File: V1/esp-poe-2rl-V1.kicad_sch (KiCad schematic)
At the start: 56 parts, among them J1 USB_C_Receptacle_USB2.0, J2 RJ45 JACK, J3 1x2P 5,08mm, J4 1x2P 5,08mm, K1 G5NB-1A-E-DC5, K2 G5NB-1A-E-DC5, Q1 UMH3N, Q2 WPM2015-3/TR, Q3 LMUN2211LT1G, Q4 MMBT2222A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

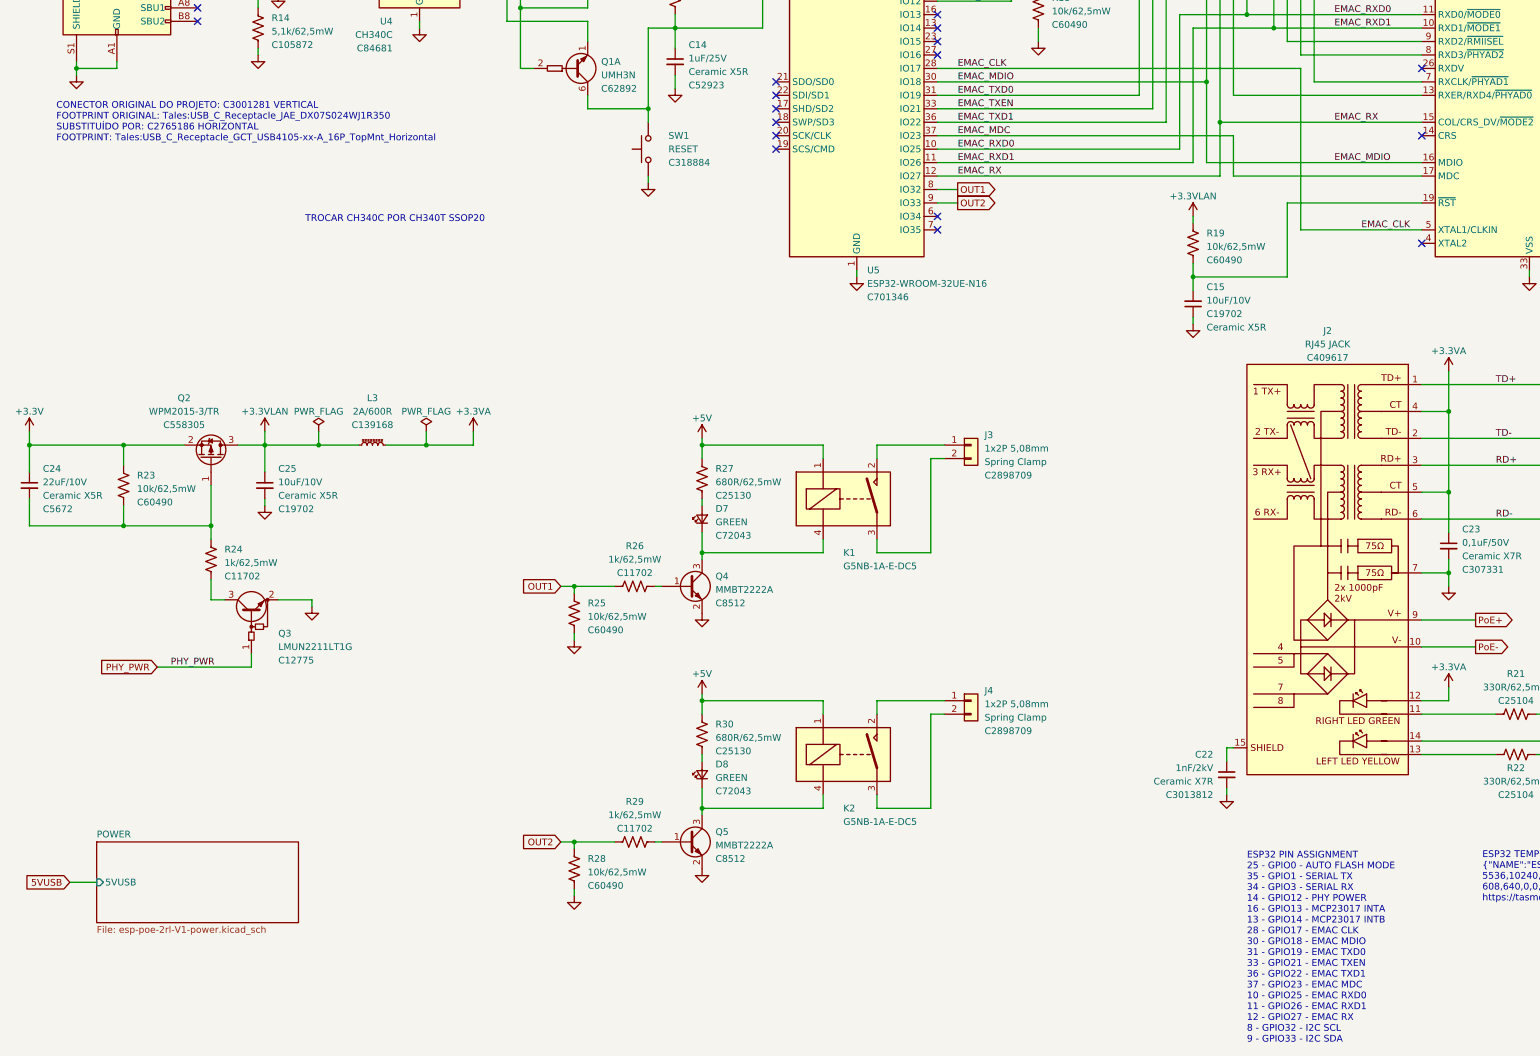
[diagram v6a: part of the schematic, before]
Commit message: Migrating layout to 4 layers
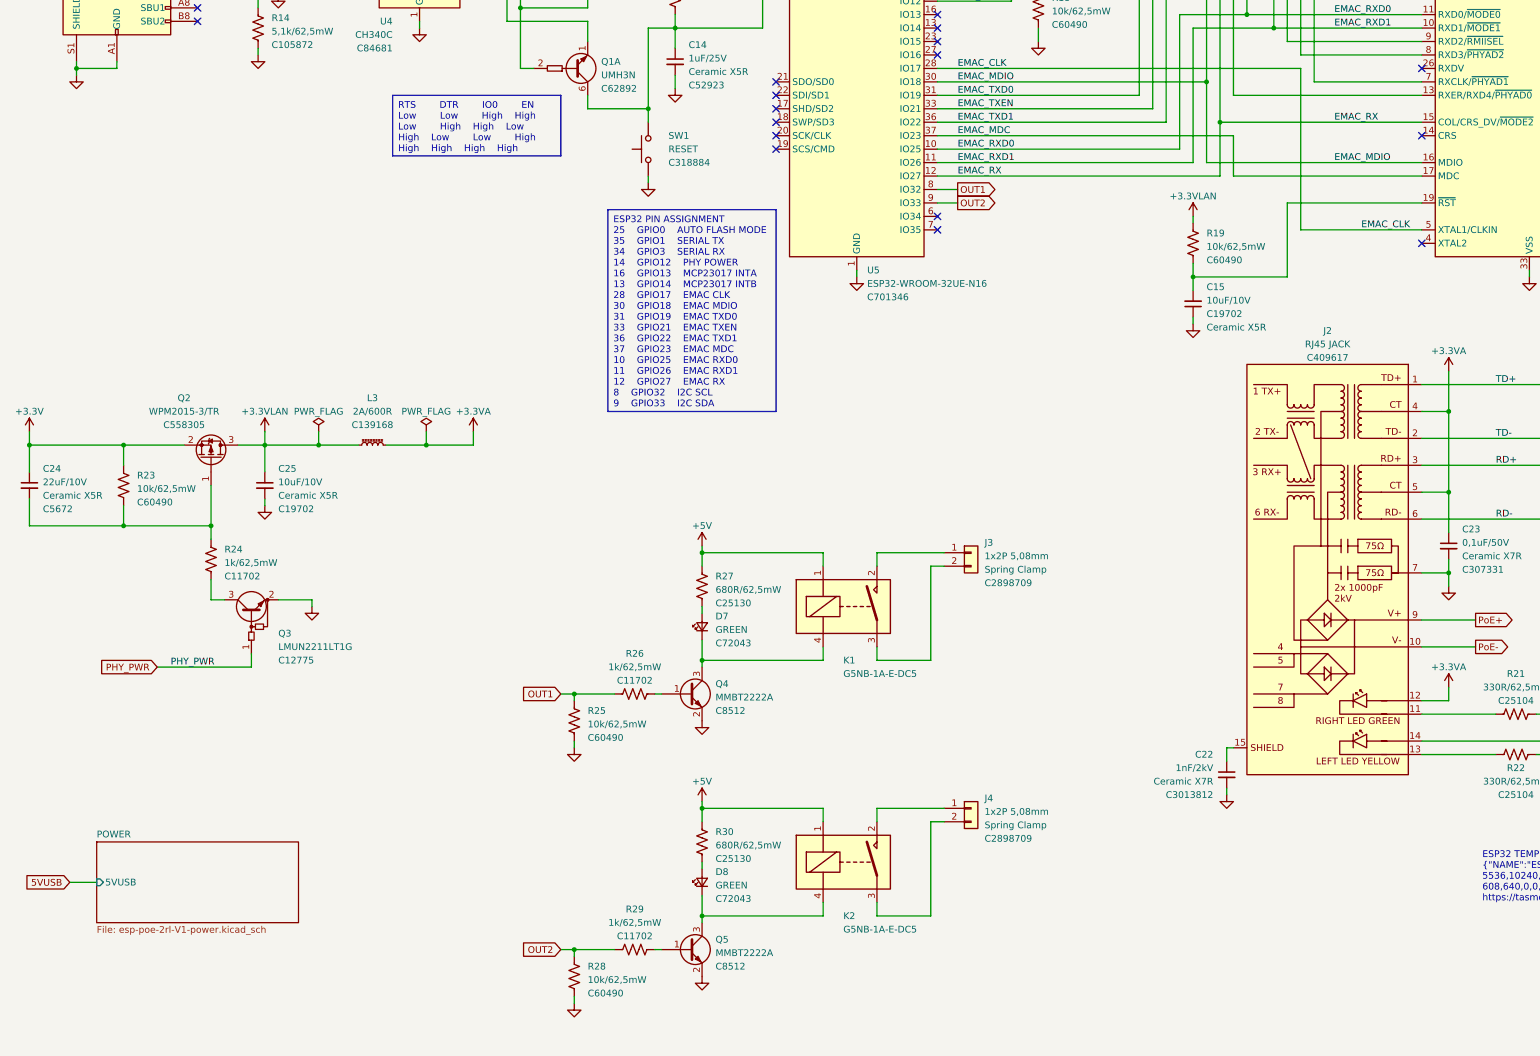
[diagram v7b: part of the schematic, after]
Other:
- note removed: "CONECTOR ORIGINAL DO PROJETO: C3001281 VERTICAL FOOTPRINT ORIGINAL: Tales:USB_C_Receptacle_JAE_DX07S024WJ1R350 SUBSTITUÍDO POR: C2765186 HORIZONTAL FOOTPRINT: Tales:USB_C_Receptacle_GCT_USB4105-xx-A_16P_TopMnt_Horizontal"
- note removed: "ESP32 PIN ASSIGNMENT 25 - GPIO0 - AUTO FLASH MODE 35 - GPIO1 - SERIAL TX 34 - GPIO3 - SERIAL RX 14 - GPIO12 - PHY POWER 16 - GPIO13 - MCP23017 INTA 13 - GPIO14 - MCP23017 INTB 28 - GPIO17 - EMAC CLK 30 - GPIO18 - EMAC MDIO 31 - GPIO19 - EMAC TXD0 33 - GPIO21 - EMAC TXEN 36 - GPIO22 - EMAC TXD1 37 - GPIO23 - EMAC MDC 10 - GPIO25 - EMAC RXD0 11 - GPIO26 - EMAC RXD1 12 - GPIO27 - EMAC RX 8 - GPIO32 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"
- note removed: "TROCAR CH340C POR CH340T SSOP20"
- moved on the sheet: D7, D8, J3, J4, K1, K2, Q4, Q5, R25, R26, R27, R28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

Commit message: PCB dev
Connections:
- net +3.3VLAN: now also RN1.6 (R3.2); no longer RN1.5 (R4.2)
- net EMAC_RXD0: now also RN1.3 (R3.1); no longer RN1.4 (R4.1)
- net GND: now also RN1.5 (R4.2); no longer RN1.6 (R3.2)
- net at U6.13 (RXER/RXD4/~{PHYAD0}): now also RN1.4 (R4.1); no longer RN1.3 (R3.1)
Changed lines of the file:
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@@
   (junction (at 359.41 85.09) (diameter 0) (color 0 0 0 0)
   )
+  (junction (at 252.73 46.99) (diameter 0) (color 0 0 0 0)
+  )
   (junction (at 128.27 259.08) (diameter 0) (color 0 0 0 0)
   )
@@
   (junction (at 317.5 29.21) (diameter 0) (color 0 0 0 0)
   )
+  (junction (at 252.73 82.55) (diameter 0) (color 0 0 0 0)
+  )
   (junction (at 245.11 132.08) (diameter 0) (color 0 0 0 0)
   )
@@
   (junction (at 311.15 46.99) (diameter 0) (color 0 0 0 0)
   )
-  (junction (at 255.27 82.55) (diameter 0) (color 0 0 0 0)
-  )
   (junction (at 63.5 40.64) (diameter 0) (color 0 0 0 0)
   )
@@
   )
   (junction (at 387.35 142.24) (diameter 0) (color 0 0 0 0)
-  )
-  (junction (at 255.27 46.99) (diameter 0) (color 0 0 0 0)
   )
   (junction (at 308.61 46.99) (diameter 0) (color 0 0 0 0)
@@
     (stroke (width 0) (type default))
   )
+  (wire (pts (xy 252.73 59.69) (xy 252.73 82.55))
+    (stroke (width 0) (type default))
+  )
   (wire (pts (xy 387.35 96.52) (xy 389.89 96.52))
     (stroke (width 0) (type default))
@@
     (stroke (width 0) (type default))
   )
-  (wire (pts (xy 255.27 82.55) (xy 288.29 82.55))
-    (stroke (width 0) (type default))
-  )
   (wire (pts (xy 288.29 167.64) (xy 359.41 167.64))
     (stroke (width 0) (type default))
@@
     (stroke (width 0) (type default))
   )
-  (wire (pts (xy 260.35 46.99) (xy 255.27 46.99))
+  (wire (pts (xy 250.19 46.99) (xy 252.73 46.99))
     (stroke (width 0) (type default))
   )
@@
     (stroke (width 0) (type default))
   )
-  (wire (pts (xy 255.27 46.99) (xy 250.19 46.99))
-    (stroke (width 0) (type default))
-  )
   (wire (pts (xy 63.5 40.64) (xy 80.01 40.64))
     (stroke (width 0) (type default))
@@
     (stroke (width 0) (type default))
   )
+  (wire (pts (xy 252.73 82.55) (xy 288.29 82.55))
+    (stroke (width 0) (type default))
+  )
   (wire (pts (xy 25.4 179.07) (xy 43.18 179.07))
     (stroke (width 0) (type default))
@@
     (stroke (width 0) (type default))
   )
+  (wire (pts (xy 255.27 43.18) (xy 265.43 43.18))
+    (stroke (width 0) (type default))
+  )
   (wire (pts (xy 262.89 87.63) (xy 288.29 87.63))
     (stroke (width 0) (type default))
@@
     (stroke (width 0) (type default))
   )
-  (wire (pts (xy 252.73 59.69) (xy 252.73 97.79))
+  (wire (pts (xy 255.27 59.69) (xy 255.27 97.79))
     (stroke (width 0) (type default))
   )
@@
     (stroke (width 0) (type default))
   )
-  (wire (pts (xy 252.73 43.18) (xy 265.43 43.18))
-    (stroke (width 0) (type default))
-  )
   (wire (pts (xy 317.5 27.94) (xy 317.5 29.21))
     (stroke (width 0) (type default))
@@
     (stroke (width 0) (type default))
   )
-  (wire (pts (xy 242.57 82.55) (xy 255.27 82.55))
+  (wire (pts (xy 242.57 82.55) (xy 252.73 82.55))
     (stroke (width 0) (type default))
   )
@@
     (stroke (width 0) (type default))
   )
+  (wire (pts (xy 252.73 46.99) (xy 252.73 49.53))
+    (stroke (width 0) (type default))
+  )
   (wire (pts (xy 245.11 110.49) (xy 245.11 85.09))
     (stroke (width 0) (type default))
@@
     (stroke (width 0) (type default))
   )
-  (wire (pts (xy 255.27 59.69) (xy 255.27 82.55))
-    (stroke (width 0) (type default))
-  )
   (wire (pts (xy 143.51 60.96) (xy 143.51 40.64))
     (stroke (width 0) (type default))
@@
     (stroke (width 0) (type default))
   )
+  (wire (pts (xy 252.73 46.99) (xy 260.35 46.99))
+    (stroke (width 0) (type default))
+  )
   (wire (pts (xy 25.4 173.99) (xy 25.4 179.07))
     (stroke (width 0) (type default))
@@
     (stroke (width 0) (type default))
   )
-  (wire (pts (xy 252.73 97.79) (xy 288.29 97.79))
+  (wire (pts (xy 255.27 97.79) (xy 288.29 97.79))
     (stroke (width 0) (type default))
   )
@@
     (stroke (width 0) (type default))
   )
-  (wire (pts (xy 252.73 43.18) (xy 252.73 49.53))
+  (wire (pts (xy 255.27 43.18) (xy 255.27 49.53))
     (stroke (width 0) (type default))
   )
@@
     (stroke (width 0) (type default))
   )
-  (wire (pts (xy 255.27 49.53) (xy 255.27 46.99))
-    (stroke (width 0) (type default))
-  )
